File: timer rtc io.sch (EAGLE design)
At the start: 42 parts, among them IC10 74HC00, IC11 74HC08, IC12 74HC32, IC13 74HC138, IC14 74HC573, IC15 74HC573, IC16 74HC573, IC17 74HC573, IC18 74HC11, IC19 74HC590, IC2 74HC245, IC20 74HC688, IC3 74HC245, IC4 74HC688, IC5 74HC688, IC6 74HC138, IC7 74HC573, IC8 74HC245, IC9 74HC688, Q1 32.768KHz, U1 BQ4845, Y1 4.096MHz

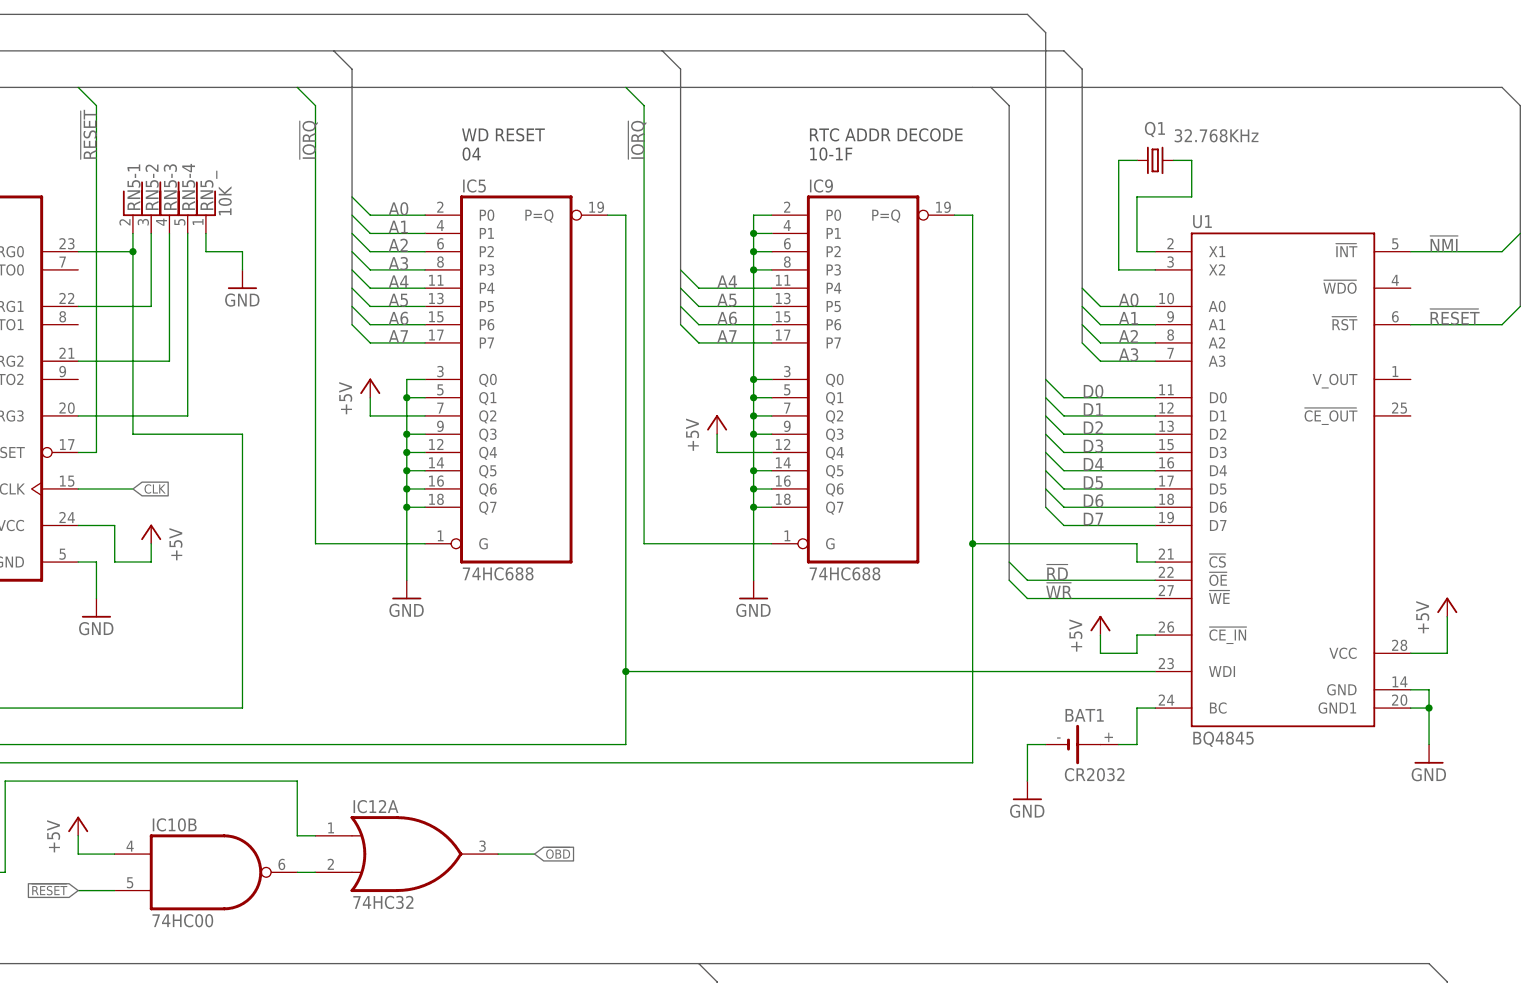
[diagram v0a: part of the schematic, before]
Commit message: BQ4845 INT pin to CTC TRG3 for vectored RTC interrupts
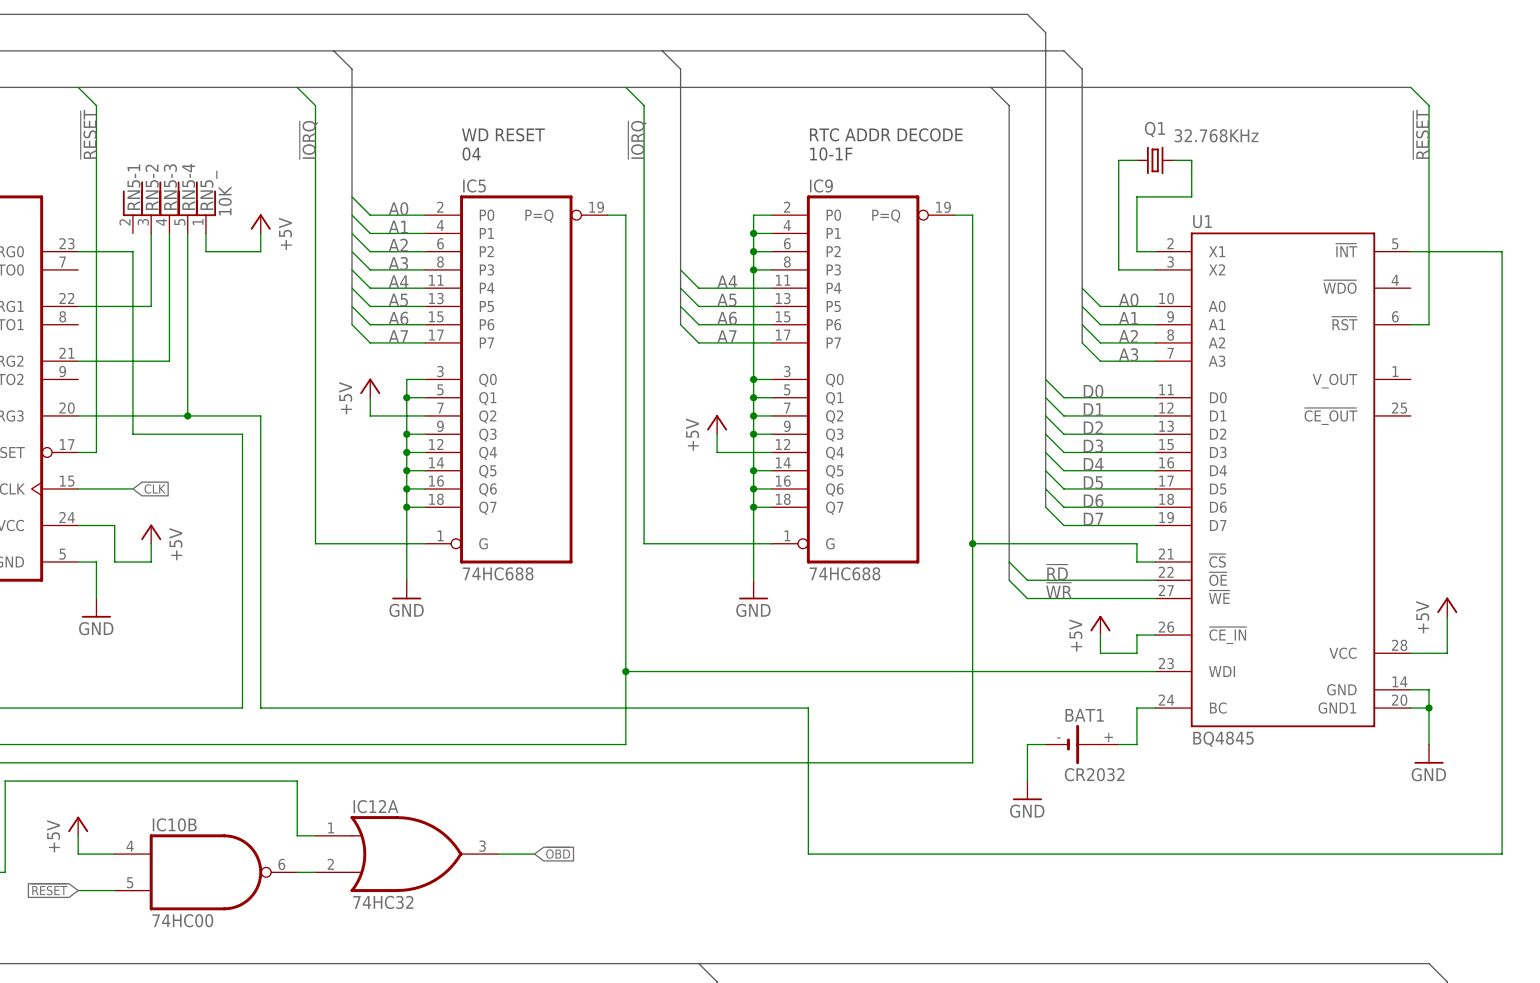
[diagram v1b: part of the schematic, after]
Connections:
- removed net !NMI!: U1.!INT!
- net +5V: now also RN5_.1
- net GND: no longer RN5_.1
- net N$59: no longer RN5-1.1
- net N$62: now also U1.!INT!
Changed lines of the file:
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@@
 <part name="GND13" library="supply1" deviceset="GND" device=""/>
 <part name="RN5" library="resistor-net" deviceset="RNX4" device="" value="10K"/>
-<part name="GND14" library="supply1" deviceset="GND" device=""/>
 <part name="IC6" library="74xx-us" deviceset="74*138" device="N" technology="LS" value="74HC138"/>
 <part name="IC7" library="74xx-us" deviceset="74*573" device="N" technology="HC" value="74HC573"/>
@@
 <part name="IC10" library="74xx-us" deviceset="74*00" device="N" technology="LS" value="74HC00"/>
 <part name="P+17" library="supply1" deviceset="+5V" device=""/>
+<part name="P+18" library="supply1" deviceset="+5V" device=""/>
 </parts>
 <sheets>
@@
 <attribute name="NAME" x="283.718" y="132.588" size="1.778" layer="95" rot="MR90"/>
 </instance>
-<instance part="GND14" gate="1" x="292.1" y="121.92" smashed="yes">
-<attribute name="VALUE" x="289.56" y="119.38" size="1.778" layer="96"/>
-</instance>
 <instance part="IC6" gate="A" x="160.02" y="-33.02" smashed="yes">
 <attribute name="NAME" x="149.86" y="-22.225" size="1.778" layer="95"/>
@@
 <instance part="P+17" gate="1" x="269.24" y="48.26" smashed="yes">
 <attribute name="VALUE" x="266.7" y="43.18" size="1.778" layer="96" rot="R90"/>
+</instance>
+<instance part="P+18" gate="1" x="294.64" y="132.08" smashed="yes" rot="MR0">
+<attribute name="VALUE" x="297.18" y="127" size="1.778" layer="96" rot="MR90"/>
 </instance>
 </instances>
@@
 </segment>
 <segment>
-<wire x1="396.24" y1="149.86" x2="467.36" y2="149.86" width="0.762" layer="92"/>
-<wire x1="467.36" y1="149.86" x2="469.9" y2="147.32" width="0.762" layer="92"/>
-<wire x1="469.9" y1="147.32" x2="469.9" y2="119.38" width="0.762" layer="92"/>
+<wire x1="396.24" y1="149.86" x2="454.66" y2="149.86" width="0.762" layer="92"/>
 </segment>
 <segment>
@@
 </segment>
 <segment>
-<pinref part="RN5" gate="_" pin="1"/>
-<pinref part="GND14" gate="1" pin="GND"/>
-<wire x1="292.1" y1="124.46" x2="292.1" y2="127" width="0.1524" layer="91"/>
-<wire x1="292.1" y1="127" x2="287.02" y2="127" width="0.1524" layer="91"/>
-<wire x1="287.02" y1="127" x2="287.02" y2="129.54" width="0.1524" layer="91"/>
-</segment>
-<segment>
 <pinref part="SW5" gate="A" pin="8"/>
 <pinref part="GND20" gate="1" pin="GND"/>
@@
 <wire x1="269.24" y1="43.18" x2="269.24" y2="45.72" width="0.1524" layer="91"/>
 </segment>
+<segment>
+<pinref part="RN5" gate="_" pin="1"/>
+<wire x1="287.02" y1="129.54" x2="287.02" y2="127" width="0.1524" layer="91"/>
+<pinref part="P+18" gate="1" pin="+5V"/>
+<wire x1="287.02" y1="127" x2="294.64" y2="127" width="0.1524" layer="91"/>
+<wire x1="294.64" y1="127" x2="294.64" y2="129.54" width="0.1524" layer="91"/>
+</segment>
 </net>
 <net name="A1" class="0">
@@
 <net name="!RESET!" class="0">
 <segment>
-<pinref part="U1" gate="G$1" pin="!RST!"/>
-<wire x1="454.66" y1="116.84" x2="467.36" y2="116.84" width="0.1524" layer="91"/>
-<wire x1="467.36" y1="116.84" x2="469.9" y2="119.38" width="0.1524" layer="91"/>
-<label x="457.2" y="116.84" size="1.778" layer="95"/>
-</segment>
-<segment>
 <wire x1="269.24" y1="149.86" x2="271.78" y2="147.32" width="0.1524" layer="91"/>
 <wire x1="271.78" y1="147.32" x2="271.78" y2="99.06" width="0.1524" layer="91"/>
@@
 <wire x1="73.66" y1="2.54" x2="76.2" y2="5.08" width="0.1524" layer="91"/>
 <label x="35.56" y="2.54" size="1.27" layer="95" rot="R180" xref="yes"/>
+</segment>
+<segment>
+<wire x1="454.66" y1="149.86" x2="457.2" y2="147.32" width="0.1524" layer="91"/>
+<wire x1="457.2" y1="147.32" x2="457.2" y2="116.84" width="0.1524" layer="91"/>
+<pinref part="U1" gate="G$1" pin="!RST!"/>
+<wire x1="457.2" y1="116.84" x2="454.66" y2="116.84" width="0.1524" layer="91"/>
+<label x="457.2" y="139.7" size="1.778" layer="95" rot="R90"/>
 </segment>
 </net>
@@
 </net>
 <net name="!NMI!" class="0">
-<segment>
-<pinref part="U1" gate="G$1" pin="!INT!"/>
-<wire x1="454.66" y1="127" x2="467.36" y2="127" width="0.1524" layer="91"/>
-<wire x1="467.36" y1="127" x2="469.9" y2="129.54" width="0.1524" layer="91"/>
-<label x="457.2" y="127" size="1.778" layer="95"/>
-</segment>
 <segment>
 <wire x1="35.56" y1="5.08" x2="73.66" y2="5.08" width="0.1524" layer="91"/>
@@
 <wire x1="292.1" y1="101.6" x2="276.86" y2="101.6" width="0.1524" layer="91"/>
 <pinref part="IC1" gate="1" pin="TRG0"/>
-<pinref part="RN5" gate="-1" pin="1"/>
 <wire x1="269.24" y1="127" x2="276.86" y2="127" width="0.1524" layer="91"/>
-<wire x1="276.86" y1="127" x2="276.86" y2="129.54" width="0.1524" layer="91"/>
 <wire x1="276.86" y1="101.6" x2="276.86" y2="127" width="0.1524" layer="91"/>
-<junction x="276.86" y="127"/>
 <pinref part="IC11" gate="C" pin="O"/>
 <wire x1="292.1" y1="63.5" x2="190.5" y2="63.5" width="0.1524" layer="91"/>
@@
 <wire x1="269.24" y1="104.14" x2="284.48" y2="104.14" width="0.1524" layer="91"/>
 <wire x1="284.48" y1="104.14" x2="284.48" y2="129.54" width="0.1524" layer="91"/>
-</segment>
-</net>
+<wire x1="284.48" y1="104.14" x2="294.64" y2="104.14" width="0.1524" layer="91"/>
+<wire x1="294.64" y1="104.14" x2="294.64" y2="63.5" width="0.1524" layer="91"/>
+<junction x="284.48" y="104.14"/>
+<wire x1="294.64" y1="63.5" x2="370.84" y2="63.5" width="0.1524" layer="91"/>
+<wire x1="370.84" y1="63.5" x2="370.84" y2="43.18" width="0.1524" layer="91"/>
+<wire x1="370.84" y1="43.18" x2="467.36" y2="43.18" width="0.1524" layer="91"/>
+<wire x1="467.36" y1="43.18" x2="467.36" y2="127" width="0.1524" layer="91"/>
+<pinref part="U1" gate="G$1" pin="!INT!"/>
+<wire x1="467.36" y1="127" x2="454.66" y2="127" width="0.1524" layer="91"/>
+</segment>
+</net>

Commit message: Functional design
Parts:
- removed IC1: (no value), zilog:Z80CTC
- removed IC10: 74HC00, 74xx-us:74LS00N
- removed IC11: 74HC08, 74xx-us:74LS08N
- removed IC12: 74HC32, 74xx-us:74LS32N
- removed IC18: 74HC11, 74xx-us:74LS11N
- removed IC19: 74HC590, 74xx-us:74LS590N
- removed IC2: 74HC245, 74xx-us:74LS245N
- removed IC4, IC5, IC9: 74HC688, 74xx-us:74LS688N
- removed Q1: 32.768KHz, crystal:CRYSTALTC38H
- removed Q2: (no value), Toms Library:2N7000
- added BUS: (no value), con-ml:ML40E
- added C1: 220uF, rcl:CPOL-EUE3.5-8
- added C10, C11, C12, C13, C14, C15, C16, C17, C18, C19, C2, C20, C21, C22, C23, C24, C3, C4, C5, C6, C7, C8, C9: 100nF, rcl:C-EU050-025X075
- added R2: 1K, rcl:R-EU_0207/10
- added T1: BC547, transistor:BC547
- added U10, U4, U8: 74HC688, 74xx-us:74LS688N
- added U11: 74LS30N, 74xx-us:74LS30N
- added U12: 74LS00N, 74xx-us:74LS00N
- added U13: 74HC32, 74xx-us:74LS32N
- added U14: 74HC04, 74xx-us:74LS04N
- added U5: (no value), zilog:Z80CTC
- added U6: 74HC74, 74xx-us:74LS74N
- added U7: 74HC590, 74xx-us:74LS590N
- added U9: BQ4845, Z80 clock:BQ4845P
- added X1: 32.768KHz, crystal:CRYSTALTC38H
- JP1: device jumper:JP2Q -> jumper:JP3Q
- RN2: device resistor-net:RNX8 -> resistor-net:RNX4
- RN5: device resistor-net:RNX4 -> resistor-net:RNX8
- U1: value BQ4845 -> 74HC245; device Z80 clock:BQ4845P -> 74xx-us:74LS245N
- renumbered IC13 to U16, IC14 to U18, IC15 to U19, IC16 to U20, IC17 to U21, IC20 to U15, IC3 to U2, IC6 to U17, IC7 to U22, IC8 to U3
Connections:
- removed net !OBD!: IC12A.O, IC2A.G
- removed net N$53: IC10B.O, IC12A.I1
- removed net N$60: IC12A.I0, IC18C.O
- new net !NMI!: BUS-12.S
- new net !WAIT!: BUS-10.S
- new net DIR: U12A.O, U1A.DIR
- new net N$65: BUS-24.S, U1A.A7
- new net N$66: BUS-25.S, U1A.A6
- new net N$67: BUS-26.S, U1A.A5
- new net N$68: BUS-27.S, U1A.A4
- new net N$69: BUS-28.S, U1A.A3
- new net N$70: BUS-29.S, U1A.A2
- new net N$71: BUS-30.S, U1A.A1
- new net N$72: BUS-33.S, U2A.A8
- new net N$73: BUS-34.S, U2A.A7
- new net N$74: BUS-35.S, U2A.A6
- new net N$75: BUS-36.S, U2A.A5
- new net N$76: BUS-37.S, U2A.A4
- new net N$77: BUS-38.S, U2A.A3
- new net N$78: BUS-39.S, U2A.A2
- new net N$79: BUS-40.S, U2A.A1
- new net N$80: BUS-14.S, U3A.A1
- new net N$81: BUS-13.S, U3A.A2
- new net N$82: BUS-9.S, U3A.A3
- new net N$83: BUS-8.S, U3A.A4
- new net N$84: BUS-7.S, U3A.A5
- new net N$85: BUS-5.S, U3A.A8
- new net N$86: R2.2, T1.B
- net !INT!: now also BUS-11.S, U5.INT; no longer IC1.INT
- net !IORQ!: now also U10A.G, U13B.I0, U13D.I0, U15A.G, U4A.G, U5.IORQ, U8A.G; no longer IC1.IORQ, IC12B.I0, IC12D.I0, IC4A.G, IC5A.G, IC9A.G
- net !M1!: now also U5.M1; no longer IC1.M1
- net !RD!: now also U13B.I1, U14F.I, U5.RD, U9.!OE!; no longer IC1.RD, IC12B.I1, IC2A.DIR, U1.!OE!
- net !RESET!: now also BUS-6.S, U12D.I1, U14A.I, U5.RESET, U6A.CLR, U6B.CLR, U7A.CCLR, U9.!RST!; no longer IC1.RESET, IC10A.I1, IC10B.I1, IC19A.CCLR, U1.!RST!
- net !WR!: now also U13D.I1, U9.!WE!; no longer IC12D.I1, U1.!WE!
- net +5V: now also BUS-2.S, BUS-4.S, C1.+, C10.1, C11.1, C12.1, C13.1, C14.1, C15.1, C16.1, C17.1, C18.1, C19.1, C2.1, C20.1, C21.1, C22.1, C23.1, C24.1, C3.1, C4.1, C5.1, C6.1, C7.1, C8.1, C9.1, R1.2, RN2_.1, RN3_.1, RN6_.1, U10A.Q2, U10P.VCC, U11P.VCC, U12P.VCC, U13P.VCC, U14P.VCC, U15P.VCC, U16P.VCC, U17P.VCC, U18P.VCC, U19P.VCC, U1P.VCC, U20P.VCC, U21P.VCC, U22P.VCC, U2P.VCC, U3P.VCC, U4P.VCC, U5.IEI, U5.VCC, U6A.PRE, U6B.PRE, U6P.VCC, U7P.VCC, U8A.Q4, U8P.VCC, U9.!CE_IN!, U9.VCC; no longer IC1.IEI, IC1.VCC, IC10B.I0, IC5A.Q2, IC9A.Q4, R1.1, SW6.10, SW6.11, SW6.12, SW6.13, SW6.14, SW6.15, SW6.16, SW6.9, SW7.10, SW7.11, SW7.12, SW7.13, SW7.14, SW7.15, SW7.16, SW7.9, SW8.10, SW8.11, SW8.12, SW8.13, SW8.14, SW8.15, SW8.16, SW8.9, U1.!CE_IN!, U1.VCC
- net A0: now also U10A.P0, U5.CS0, U9.A0; no longer IC1.CS0, IC5A.P0, U1.A0
- net A1: now also U10A.P1, U5.CS1, U9.A1; no longer IC1.CS1, IC5A.P1, U1.A1
- net A2: now also U10A.P2, U4A.P2, U9.A2; no longer IC4A.P2, IC5A.P2, U1.A2
- net A3: now also U10A.P3, U4A.P3, U9.A3; no longer IC4A.P3, IC5A.P3, U1.A3
- net A4: now also U10A.P4, U4A.P4, U8A.P4; no longer IC4A.P4, IC5A.P4, IC9A.P4
- net A5: now also U10A.P5, U4A.P5, U8A.P5; no longer IC4A.P5, IC5A.P5, IC9A.P5
- net A6: now also U10A.P6, U4A.P6, U8A.P6; no longer IC4A.P6, IC5A.P6, IC9A.P6
- net A7: now also U10A.P7, U4A.P7, U8A.P7; no longer IC4A.P7, IC5A.P7, IC9A.P7
- net CLK: now also U5.CLK; no longer IC1.CLK
- net D0: now also RN1-1.1, U1A.B1, U5.D0, U9.D0; no longer IC1.D0, IC2A.B1, RN6-1.1, U1.D0
- net D1: now also RN1-2.1, U1A.B2, U5.D1, U9.D1; no longer IC1.D1, IC2A.B2, RN6-2.1, U1.D1
- net D2: now also RN1-3.1, U1A.B3, U5.D2, U9.D2; no longer IC1.D2, IC2A.B3, RN6-3.1, U1.D2
- net D3: now also RN1-4.1, U1A.B4, U5.D3, U9.D3; no longer IC1.D3, IC2A.B4, RN6-4.1, U1.D3
- net D4: now also RN1-5.1, U1A.B5, U5.D4, U9.D4; no longer IC1.D4, IC2A.B5, RN6-5.1, U1.D4
- net D5: now also RN1-6.1, U1A.B6, U5.D5, U9.D5; no longer IC1.D5, IC2A.B6, RN6-6.1, U1.D5
- net D6: now also RN1-7.1, U1A.B7, U5.D6, U9.D6; no longer IC1.D6, IC2A.B7, RN6-7.1, U1.D6
- net D7: now also RN1-8.1, U1A.B8, U5.D7, U9.D7; no longer IC1.D7, IC2A.B8, RN6-8.1, U1.D7
- net GND: now also BUS-1.S, BUS-3.S, C1.-, C10.2, C11.2, C12.2, C13.2, C14.2, C15.2, C16.2, C17.2, C18.2, C19.2, C2.2, C20.2, C21.2, C22.2, C23.2, C24.2, C3.2, C4.2, C5.2, C6.2, C7.2, C8.2, C9.2, SW6.10, SW6.11, SW6.12, SW6.13, SW6.14, SW6.15, SW6.16, SW6.9, SW7.10, SW7.11, SW7.12, SW7.13, SW7.14, SW7.15, SW7.16, SW7.9, SW8.10, SW8.11, SW8.12, SW8.13, SW8.14, SW8.15, SW8.16, SW8.9, T1.E, U10A.Q0, U10A.Q1, U10A.Q3, U10A.Q4, U10A.Q5, U10A.Q6, U10A.Q7, U10P.GND, U11P.GND, U12B.I0, U12B.I1, U12C.I0, U12C.I1, U12P.GND, U13A.I0, U13A.I1, U13C.I0, U13C.I1, U13P.GND, U14B.I, U14C.I, U14D.I, U14E.I, U14P.GND, U15P.GND, U16P.GND, U17P.GND, U18P.GND, U19P.GND, U1P.GND, U20P.GND, U21P.GND, U22P.GND, U2P.GND, U3P.GND, U4A.P0, U4A.P1, U4A.Q0, U4A.Q1, U4A.Q2, U4A.Q3, U4A.Q4, U4A.Q5, U4A.Q6, U4A.Q7, U4P.GND, U5.GND, U6P.GND, U7A.CCKEN, U7A.G, U7A.RCK, U7P.GND, U8A.P0, U8A.P1, U8A.P2, U8A.P3, U8A.Q0, U8A.Q1, U8A.Q2, U8A.Q3, U8A.Q5, U8A.Q6, U8A.Q7, U8P.GND, U9.GND, U9.GND1; no longer IC1.GND, IC10C.I0, IC10C.I1, IC10D.I0, IC10D.I1, IC11B.I0, IC11B.I1, IC11D.I0, IC11D.I1, IC12C.I0, IC12C.I1, IC19A.CCKEN, IC19A.G, IC4A.P0, IC4A.P1, IC4A.Q0, IC4A.Q1, IC4A.Q2, IC4A.Q3, IC4A.Q4, IC4A.Q5, IC4A.Q6, IC4A.Q7, IC5A.Q0, IC5A.Q1, IC5A.Q3, IC5A.Q4, IC5A.Q5, IC5A.Q6, IC5A.Q7, IC9A.P0, IC9A.P1, IC9A.P2, IC9A.P3, IC9A.Q0, IC9A.Q1, IC9A.Q2, IC9A.Q3, IC9A.Q5, IC9A.Q6, IC9A.Q7, Q2.S, RN2_.1, RN3_.1, RN6_.1, U1.GND, U1.GND1, U15A.G
- net N$1: now also JP1.3, U6A.!Q, U6A.D, U6B.CLK; no longer IC19A.CLK, IC19A.RCK, Y1.OUT
- net N$11: now also U13B.O; no longer IC12B.O
- net N$12: now also RN4-1.1; no longer RN1-1.1
- net N$13: now also RN4-2.1; no longer RN1-2.1
- net N$14: now also RN4-3.1; no longer RN1-3.1
- net N$15: now also RN4-4.1; no longer RN1-4.1
- net N$16: now also RN4-5.1; no longer RN1-5.1
- net N$17: now also RN4-6.1; no longer RN1-6.1
- net N$18: now also RN4-7.1; no longer RN1-7.1
- net N$19: now also RN4-8.1; no longer RN1-8.1
- net N$2: now also U9.X1, X1.1; no longer Q1.1, U1.X1
- net N$20: now also RN5-1.1; no longer RN2-1.1
- net N$21: now also RN5-2.1; no longer RN2-2.1
- net N$22: now also RN5-3.1; no longer RN2-3.1
- net N$23: now also RN5-4.1; no longer RN2-4.1
- net N$24: now also RN5-5.1; no longer RN2-5.1
- net N$25: now also RN5-6.1; no longer RN2-6.1
- net N$26: now also RN5-7.1; no longer RN2-7.1
- net N$27: now also RN5-8.1; no longer RN2-8.1
- net N$28: now also RN6-1.1; no longer RN3-1.1
- net N$29: now also RN6-2.1; no longer RN3-2.1
- net N$3: now also U10A.P=Q, U11A.I1, U9.WDI; no longer IC18A.I1, IC5A.P=Q, U1.WDI
- net N$30: now also RN6-3.1; no longer RN3-3.1
- net N$31: now also RN6-4.1; no longer RN3-4.1
- net N$32: now also RN6-5.1; no longer RN3-5.1
- net N$33: now also RN6-6.1; no longer RN3-6.1
- net N$34: now also RN6-7.1; no longer RN3-7.1
- net N$35: now also RN6-8.1; no longer RN3-8.1
- net N$36: now also U11A.O, U12A.I0; no longer IC10A.O, U22A.C
- net N$37: now also RN3-1.1; no longer RN4-1.1
- net N$38: now also RN3-2.1; no longer RN4-2.1
- net N$39: now also RN3-3.1; no longer RN4-3.1
- net N$4: now also U9.X2, X1.2; no longer Q1.2, U1.X2
- net N$40: now also RN3-4.1; no longer RN4-4.1
- net N$41: now also RN3-5.1; no longer RN4-5.1
- net N$42: now also RN3-6.1; no longer RN4-6.1
- net N$43: now also RN3-7.1; no longer RN4-7.1
- net N$44: now also RN3-8.1; no longer RN4-8.1
- net N$45: now also U11A.I3; no longer IC18B.I0
- net N$46: now also U11A.I4; no longer IC18B.I1
- net N$47: now also U11A.I5; no longer IC18B.I2
- net N$48: now also U11A.I6; no longer IC11A.I0
- net N$49: now also BUS-23.S, U1A.A8; no longer IC1.TRG1, RN5-2.1
- net N$5: now also U11A.I0, U8A.P=Q, U9.!CS!; no longer IC18A.I0, IC9A.P=Q, U1.!CS!
- net N$50: now also RN2-3.1, U5.TRG2; no longer IC1.TRG2, RN5-3.1
- net N$51: now also U12A.I1, U14F.O; no longer IC18A.O, IC18C.I0
- net N$52: now also U13D.O; no longer IC12D.O
- net N$54: now also U11A.I7, U12D.I0; no longer IC10A.I0, IC11A.I1
- net N$55: now also R2.1; no longer Q2.G
- net N$56: now also R1.1, T1.C; no longer Q2.D, R1.2
- net N$57: now also U6A.CLK, Y1.OUT; no longer IC19A.QD
- net N$58: now also JP1.5, U6B.!Q, U6B.D; no longer IC19A.QH, JP1.3
- net N$59: now also RN2-2.1, U5.TRG1, U7A.RCO; no longer IC1.TRG0, IC11C.O
- net N$6: now also U9.BC; no longer U1.BC
- net N$62: now also RN2-4.1, U5.TRG3, U9.!INT!; no longer IC1.TRG3, RN5-4.1, U1.!INT!
- net N$63: now also JP1.6, U7A.CLK; no longer IC11C.I0
- net N$64: now also RN2-1.1, U5.TRG0; no longer IC11C.I1, U22A.1Q
- net N$7: now also U11A.I2, U4A.P=Q, U5.CE; no longer IC1.CE, IC18A.I2, IC4A.P=Q
- net N$8: now also U12D.O, U22A.C; no longer IC18B.O, IC18C.I1
- net N$9: now also U14A.O, U1A.G; no longer IC11A.O, IC18C.I2
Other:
- note added: "JP1: PERIOD CLOCK DIVIDER 1-2 ÷ 1 3-4 ÷ 2 5-6 ÷ 4"
- note removed: "CTC PRESCALER 1-2 ÷16 3-4 ÷256"
- moved on the sheet: BAT1, R1, RN1-1, RN1-2, RN1-3, RN1-4, RN1-5, RN1-6, RN1-7, RN1-8, RN1_, RN2-1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

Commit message: Fix CTC interrupt vector read
Added some more logic to allow the interrupt vector generated by the CTC to be read properly by the processor.

The direction logic did not account for M1/ and IORQ/ going low (interrupt ack), so the data buffer was never placed in to the correct direction.
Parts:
- added C25: 100nF, rcl:C-EU050-025X075
- added U23: 74HC573, 74xx-us:74HC573N
- U15: value 74HC688 -> 74HC08; device 74xx-us:74LS688N -> 74xx-us:74LS08N
- U16: value 74HC138 -> 74HC688; device 74xx-us:74LS138N -> 74xx-us:74LS688N
- U18: value 74HC573 -> 74HC138; device 74xx-us:74HC573N -> 74xx-us:74LS138N
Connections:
- new net N$61: U13C.O, U15A.I1
- new net N$87: U12A.O, U15A.I0
- net !IORQ!: now also U13C.I0, U16A.G; no longer U15A.G
- net !M1!: now also U13C.I1
- net +5V: now also C25.1, U16A.Q3, U18A.G1, U23P.VCC; no longer U15A.Q3, U16A.G1
- net A0: now also U18A.A; no longer U16A.A
- net A1: now also U18A.B; no longer U16A.B
- net A2: now also U18A.C; no longer U16A.C
- net A3: now also U16A.P3; no longer U15A.P3
- net A4: now also U16A.P4; no longer U15A.P4
- net A5: now also U16A.P5; no longer U15A.P5
- net A6: now also U16A.P6; no longer U15A.P6
- net A7: now also U16A.P7; no longer U15A.P7
- net D0: now also U22A.1Q, U23A.1D; no longer U18A.1Q, U22A.1D
- net D1: now also U22A.2Q, U23A.2D; no longer U18A.2Q, U22A.2D
- net D2: now also U22A.3Q, U23A.3D; no longer U18A.3Q, U22A.3D
- net D3: now also U22A.4Q, U23A.4D; no longer U18A.4Q, U22A.4D
- net D4: now also U22A.5Q, U23A.5D; no longer U18A.5Q, U22A.5D
- net D5: now also U22A.6Q, U23A.6D; no longer U18A.6Q, U22A.6D
- net D6: now also U22A.7Q, U23A.7D; no longer U18A.7Q, U22A.7D
- net D7: now also U22A.8Q, U23A.8D; no longer U18A.8Q, U22A.8D
- net DIR: now also U15A.O; no longer U12A.O
- net GND: now also C25.2, U15B.I0, U15B.I1, U15C.I0, U15C.I1, U15D.I0, U15D.I1, U16A.P0, U16A.P1, U16A.P2, U16A.Q0, U16A.Q1, U16A.Q2, U16A.Q4, U16A.Q5, U16A.Q6, U16A.Q7, U23A.OC, U23P.GND; no longer U13C.I0, U13C.I1, U15A.P0, U15A.P1, U15A.P2, U15A.Q0, U15A.Q1, U15A.Q2, U15A.Q4, U15A.Q5, U15A.Q6, U15A.Q7, U22A.OC
- net N$10: now also U16A.P=Q, U18A.G2A; no longer U15A.P=Q, U16A.G2A
- net N$11: now also U17A.G2B; no longer U16A.G2B
- net N$12: now also U20A.1D; no longer U19A.1D
- net N$13: now also U20A.2D; no longer U19A.2D
- net N$14: now also U20A.3D; no longer U19A.3D
- net N$15: now also U20A.4D; no longer U19A.4D
- net N$16: now also U20A.5D; no longer U19A.5D
- net N$17: now also U20A.6D; no longer U19A.6D
- net N$18: now also U20A.7D; no longer U19A.7D
- net N$19: now also U20A.8D; no longer U19A.8D
- net N$20: now also U21A.1D; no longer U20A.1D
- net N$21: now also U21A.2D; no longer U20A.2D
- net N$22: now also U21A.3D; no longer U20A.3D
- net N$23: now also U21A.4D; no longer U20A.4D
- net N$24: now also U21A.5D; no longer U20A.5D
- net N$25: now also U21A.6D; no longer U20A.6D
- net N$26: now also U21A.7D; no longer U20A.7D
- net N$27: now also U21A.8D; no longer U20A.8D
- net N$28: now also U22A.1D; no longer U21A.1D
- net N$29: now also U22A.2D; no longer U21A.2D
- net N$30: now also U22A.3D; no longer U21A.3D
- net N$31: now also U22A.4D; no longer U21A.4D
- net N$32: now also U22A.5D; no longer U21A.5D
- net N$33: now also U22A.6D; no longer U21A.6D
- net N$34: now also U22A.7D; no longer U21A.7D
- net N$35: now also U22A.8D; no longer U21A.8D
- net N$37: now also U19A.1D; no longer U18A.1D
- net N$38: now also U19A.2D; no longer U18A.2D
- net N$39: now also U19A.3D; no longer U18A.3D
- net N$40: now also U19A.4D; no longer U18A.4D
- net N$41: now also U19A.5D; no longer U18A.5D
- net N$42: now also U19A.6D; no longer U18A.6D
- net N$43: now also U19A.7D; no longer U18A.7D
- net N$44: now also U19A.8D; no longer U18A.8D
- net N$45: now also U17A.Y0, U19A.C, U19A.OC; no longer U16A.Y0, U18A.C, U18A.OC
- net N$46: now also U17A.Y1, U20A.C, U20A.OC; no longer U16A.Y1, U19A.C, U19A.OC
- net N$47: now also U17A.Y2, U21A.C, U21A.OC; no longer U16A.Y2, U20A.C, U20A.OC
- net N$48: now also U17A.Y3, U22A.C, U22A.OC; no longer U16A.Y3, U21A.C, U21A.OC
- net N$52: now also U18A.G2B; no longer U17A.G2B
- net N$54: now also U18A.Y4; no longer U17A.Y4
- net N$55: now also U23A.8Q; no longer U22A.8Q
- net N$8: now also U23A.C; no longer U22A.C
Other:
- note added: "WD POKE 04"
- note removed: "WD RESET 04"
- moved on the sheet: BUS-1, BUS-10, BUS-11, BUS-12, BUS-13, BUS-14, BUS-2, BUS-3, BUS-33, BUS-34, BUS-35, BUS-36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
